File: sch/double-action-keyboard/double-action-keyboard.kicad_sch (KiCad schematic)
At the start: 3 parts, among them J1 Conn_01x02, U1 Pico

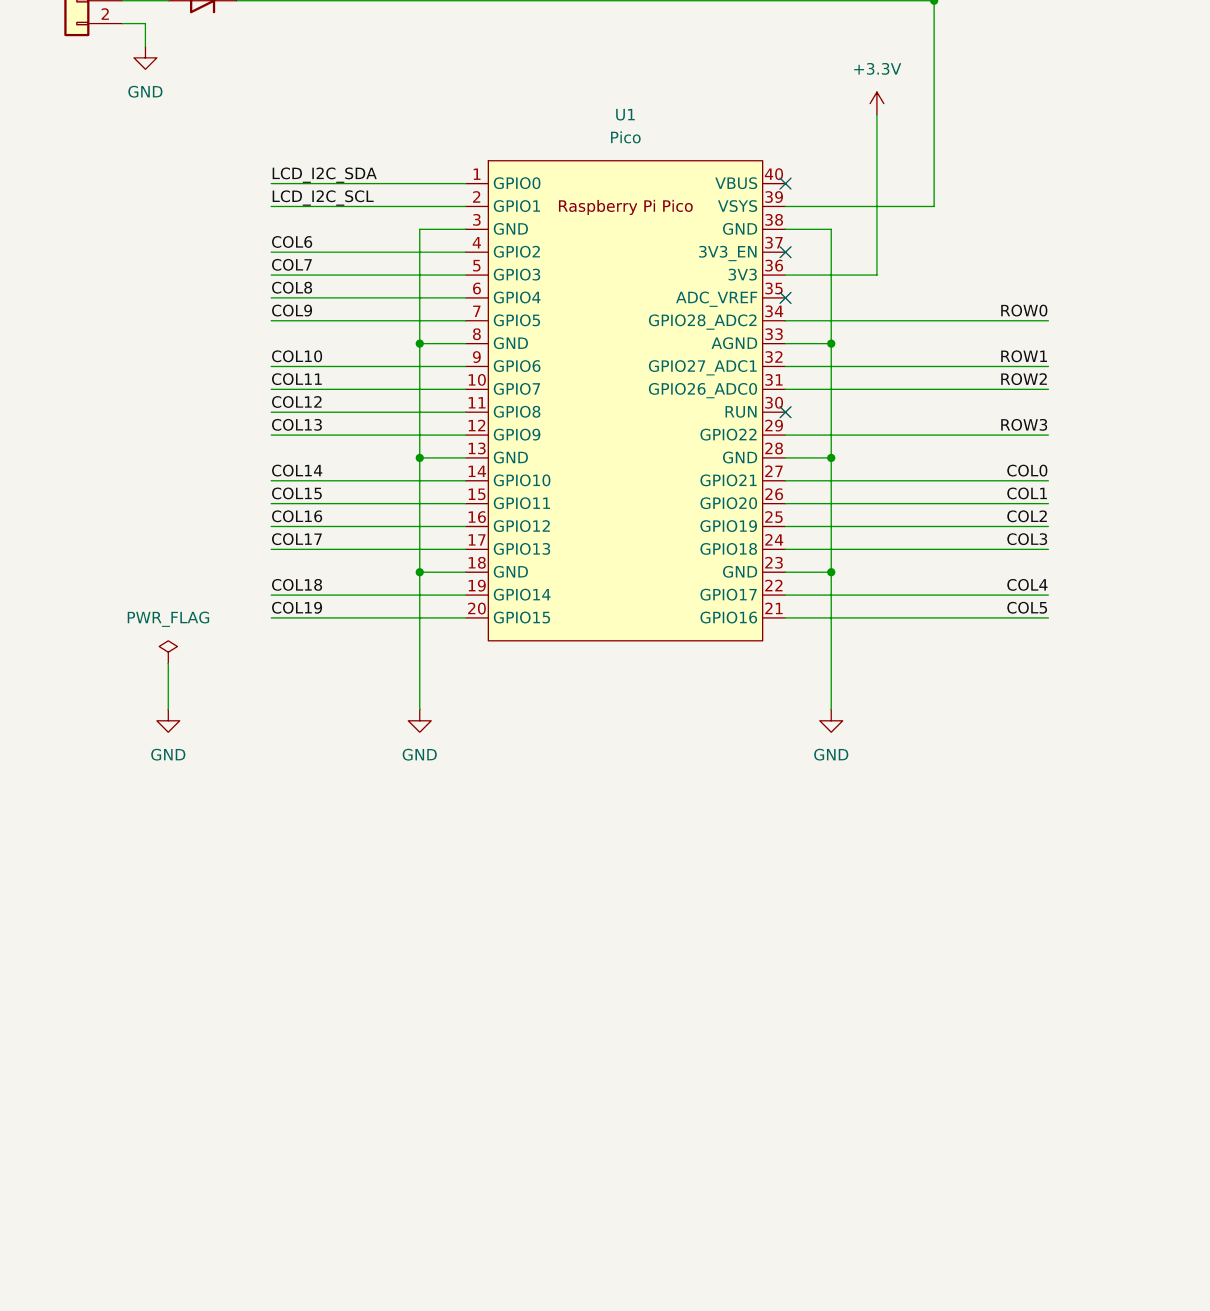
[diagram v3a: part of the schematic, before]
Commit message: picoの位置を右側に変更しました。
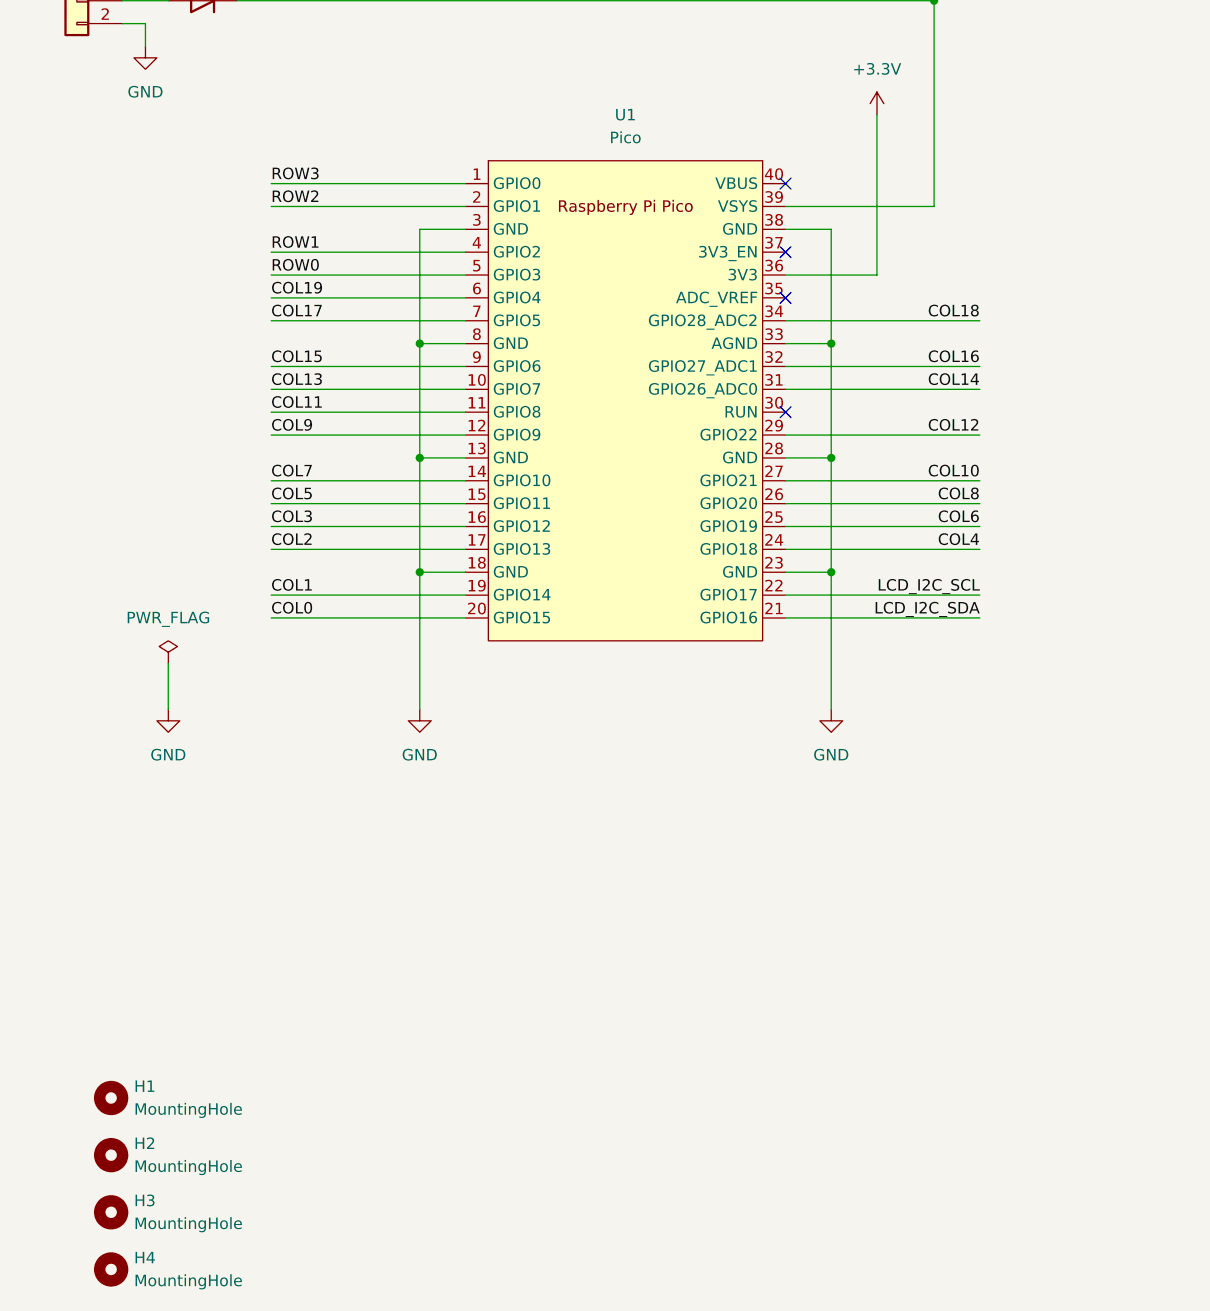
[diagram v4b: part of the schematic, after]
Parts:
- added H1, H2, H3, H4: MountingHole, MountingHole:MountingHole_2.2mm_M2, symbol Mechanical:MountingHole
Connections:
- net COL0: now also U1.20 (GPIO15); no longer U1.27 (GPIO21)
- net COL1: now also U1.19 (GPIO14); no longer U1.26 (GPIO20)
- net COL10: now also U1.27 (GPIO21); no longer U1.9 (GPIO6)
- net COL11: now also U1.11 (GPIO8); no longer U1.10 (GPIO7)
- net COL12: now also U1.29 (GPIO22); no longer U1.11 (GPIO8)
- net COL13: now also U1.10 (GPIO7); no longer U1.12 (GPIO9)
- net COL14: now also U1.31 (GPIO26_ADC0); no longer U1.14 (GPIO10)
- net COL15: now also U1.9 (GPIO6); no longer U1.15 (GPIO11)
- net COL16: now also U1.32 (GPIO27_ADC1); no longer U1.16 (GPIO12)
- net COL17: now also U1.7 (GPIO5); no longer U1.17 (GPIO13)
- net COL18: now also U1.34 (GPIO28_ADC2); no longer U1.19 (GPIO14)
- net COL19: now also U1.6 (GPIO4); no longer U1.20 (GPIO15)
- net COL2: now also U1.17 (GPIO13); no longer U1.25 (GPIO19)
- net COL3: now also U1.16 (GPIO12); no longer U1.24 (GPIO18)
- net COL4: now also U1.24 (GPIO18); no longer U1.22 (GPIO17)
- net COL5: now also U1.15 (GPIO11); no longer U1.21 (GPIO16)
- net COL6: now also U1.25 (GPIO19); no longer U1.4 (GPIO2)
- net COL7: now also U1.14 (GPIO10); no longer U1.5 (GPIO3)
- net COL8: now also U1.26 (GPIO20); no longer U1.6 (GPIO4)
- net COL9: now also U1.12 (GPIO9); no longer U1.7 (GPIO5)
- net LCD_I2C_SCL: now also U1.22 (GPIO17); no longer U1.2 (GPIO1)
- net LCD_I2C_SDA: now also U1.21 (GPIO16); no longer U1.1 (GPIO0)
- net ROW0: now also U1.5 (GPIO3); no longer U1.34 (GPIO28_ADC2)
- net ROW1: now also U1.4 (GPIO2); no longer U1.32 (GPIO27_ADC1)
- net ROW2: now also U1.2 (GPIO1); no longer U1.31 (GPIO26_ADC0)
- net ROW3: now also U1.1 (GPIO0); no longer U1.29 (GPIO22)

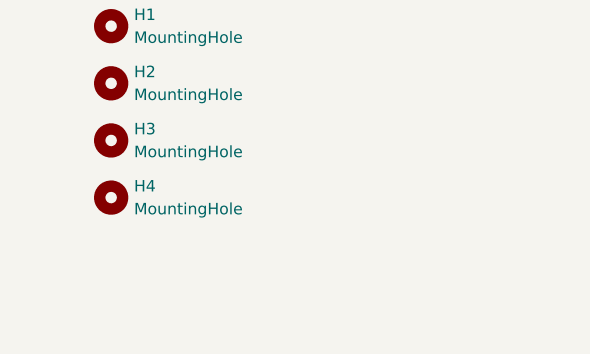
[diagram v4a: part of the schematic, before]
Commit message: ベタGNDにビアを打ちました。 空き領域にユニバーサル領域のスルーホールを追加しました。
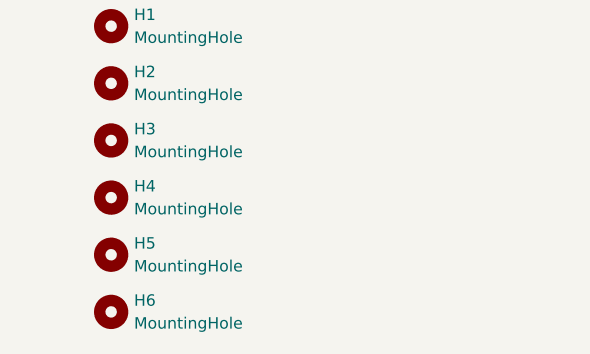
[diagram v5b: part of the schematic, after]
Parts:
- added H5, H6: MountingHole, MountingHole:MountingHole_2.2mm_M2, symbol Mechanical:MountingHole
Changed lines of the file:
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@@
+	)
+	(symbol
+		(lib_id "Mechanical:MountingHole")
+		(at 24.13 175.26 0)
+		(unit 1)
+		(exclude_from_sim yes)
+		(in_bom no)
+		(on_board yes)
+		(dnp no)
+		(fields_autoplaced yes)
+		(property "Reference" "H6"
+			(at 26.67 173.9899 0)
+			(effects
+				(font
+					(size 1.27 1.27)
+				)
+				(justify left)
+			)
+		)
+		(property "Value" "MountingHole"
+			(at 26.67 176.5299 0)
+			(effects
+				(font
+					(size 1.27 1.27)
+				)
+				(justify left)
+			)
+		)
+		(property "Footprint" "MountingHole:MountingHole_2.2mm_M2"
+			(at 24.13 175.26 0)
+			(effects
+				(font
+					(size 1.27 1.27)
+				)
+				(hide yes)
+			)
+		)
+		(property "Datasheet" "~"
+			(at 24.13 175.26 0)
+			(effects
+				(font
+					(size 1.27 1.27)
+				)
+				(hide yes)
+			)
+		)
+		(property "Description" "Mounting Hole without connection"
+			(at 24.13 175.26 0)
+			(effects
+				(font
+					(size 1.27 1.27)
+				)
+				(hide yes)
+			)
+		)
+		(instances
+			(project "double-action-keyboard"
+				(path "/99b55f71-96ca-4365-b829-4f6def2430a7"
+					(reference "H6")
+					(unit 1)
+				)
+			)
+		)
 	)
 	(symbol
@@
 					(unit 1)
 				)
+			)
+		)
+	)
+	(symbol
+		(lib_id "Mechanical:MountingHole")
+		(at 24.13 168.91 0)
+		(unit 1)
+		(exclude_from_sim yes)
+		(in_bom no)
+		(on_board yes)
+		(dnp no)
+		(fields_autoplaced yes)
+		(property "Reference" "H5"
+			(at 26.67 167.6399 0)
+			(effects
+				(font
+					(size 1.27 1.27)
+				)
+				(justify left)
+			)
+		)
+		(property "Value" "MountingHole"
+			(at 26.67 170.1799 0)
+			(effects
+				(font
+					(size 1.27 1.27)
+				)
+				(justify left)
+			)
+		)
+		(property "Footprint" "MountingHole:MountingHole_2.2mm_M2"
+			(at 24.13 168.91 0)
+			(effects
+				(font
+					(size 1.27 1.27)
+				)
+				(hide yes)
+			)
+		)
+		(property "Datasheet" "~"
+			(at 24.13 168.91 0)
+			(effects
+				(font
+					(size 1.27 1.27)
+				)
+				(hide yes)
+			)
+		)
+		(property "Description" "Mounting Hole without connection"
+			(at 24.13 168.91 0)
+			(effects
+				(font
+					(size 1.27 1.27)
+				)
+				(hide yes)
+			)
+		)
+		(instances
+			(project "double-action-keyboard"
+				(path "/99b55f71-96ca-4365-b829-4f6def2430a7"
+					(reference "H5")
+					(unit 1)
+				)
